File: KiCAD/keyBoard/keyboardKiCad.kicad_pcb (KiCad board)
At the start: 2 copper layers, 356.2 x 133.2 mm, 183 parts, among them SW1 RotaryEncoder_Switch_MP

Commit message: Fixed dimentions of the keyboard PCB, need to update 3D models
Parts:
- moved S83 413.8 mm to (0.00, 0.00)
- moved S80 398.0 mm to (0.00, 0.00)
- moved S82 397.1 mm to (0.00, 0.00)
- moved S81 390.8 mm to (0.00, 0.00)
- moved S79 390.0 mm to (0.00, 0.00)
- moved S76 382.3 mm to (0.00, 0.00)
- moved S78 380.6 mm to (0.00, 0.00)
- moved S77 374.0 mm to (0.00, 0.00)
- moved S75 364.2 mm to (0.00, 0.00)
- moved S74 357.3 mm to (0.00, 0.00)
- moved S69 350.9 mm to (0.00, 0.00)
- moved S63 336.1 mm to (0.00, 0.00)
- moved S68 331.4 mm to (0.00, 0.00)
- moved S72 329.7 mm to (0.00, 0.00)
- moved S64 328.7 mm to (0.00, 0.00)
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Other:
- board size 356.2 x 133.2 mm -> 354 x 132 mm

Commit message: Keyboard routing initially complete
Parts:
- D1, D10, D11, D12, D13, D14, D15, D16, D17, D18, D19, D2, D20, D21, D22, D23, D24, D25, D26, D27, D28, D29, D3, D30, D31, D32, D33, D34, D35, D36, D37, D38, D39, D4, D40, D41, D42, D43, D44, D45, D46, D47, D48, D49, D5, D50, D51, D52, D53, D54, D55, D56, D57, D58, D59, D6, D60, D61, D62, D63, D64, D66, D67, D68, D69, D7, D70, D71, D72, D73, D74, D75, D76, D77, D78, D79, D8, D80, D81, D82, D83, D84, D9: footprint Diode_THT:D_DO-35_SOD27_P10.16mm_Horizontal -> kbProjectLib/lcscImports:DO-35_BD2.0-L4.0-P8.00-D0.5-FD
- S1, S3, S72: footprint PCM_Switch_Keyboard_Kailh:SW_Kailh_Choc_V2_1.50u -> kbProjectLib/keyswitches:SW_Kailh_Choc_V2_1.50u
- S10, S12, S13, S14, S15, S16, S18, S19, S2, S20, S21, S22, S23, S24, S25, S26, S27, S28, S29, S30, S31, S32, S34, S35, S36, S37, S38, S39, S40, S41, S42, S43, S44, S45, S46, S47, S48, S49, S50, S51, S52, S53, S54, S55, S56, S57, S59, S60, S61, S62, S64, S65, S66, S67, S7, S70, S73, S74, S75, S76, S77, S78, S79, S8, S80, S81, S82, S83, S9: footprint PCM_Switch_Keyboard_Kailh:SW_Kailh_Choc_V2_1.00u -> kbProjectLib/keyswitches:SW_Kailh_Choc_V2_1.00u
- S11, S17, S58: footprint PCM_Switch_Keyboard_Kailh:SW_Kailh_Choc_V2_1.25u -> kbProjectLib/keyswitches:SW_Kailh_Choc_V2_1.25u
- S33: footprint PCM_Switch_Keyboard_Kailh:SW_Kailh_Choc_V2_6.25u -> kbProjectLib/keyswitches:SW_Kailh_Choc_V2_6.25u
- S4: footprint PCM_Switch_Keyboard_Kailh:SW_Kailh_Choc_V2_1.75u -> kbProjectLib/keyswitches:SW_Kailh_Choc_V2_1.75u
- S5, S68: footprint PCM_Switch_Keyboard_Kailh:SW_Kailh_Choc_V2_2.25u -> kbProjectLib/keyswitches:SW_Kailh_Choc_V2_2.25u
- S6, S69, S71: footprint PCM_Switch_Keyboard_Kailh:SW_Kailh_Choc_V2_2.00u -> kbProjectLib/keyswitches:SW_Kailh_Choc_V2_2.00u
- S63: footprint PCM_Switch_Keyboard_Kailh:SW_Kailh_Choc_V2_2.75u -> kbProjectLib/keyswitches:SW_Kailh_Choc_V2_2.75u
- SW1: footprint Rotary_Encoder:RotaryEncoder_Alps_EC11E-Switch_Vertical_H20mm -> kbProjectLib/lcscImports:SW-TH_EC11XXXXXXXX
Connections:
- S10 pad 1: ROW4 -> ROW5
- S11 pad 1: ROW5 -> ROW6
- S54 pad 1: ROW1 -> ROW2
- S55 pad 1: ROW2 -> ROW3
- S56 pad 1: ROW3 -> ROW4
- S57 pad 1: ROW4 -> ROW5
- S58 pad 1: ROW5 -> ROW6
- S7 pad 1: ROW1 -> ROW2
- S8 pad 1: ROW2 -> ROW3
- S9 pad 1: ROW3 -> ROW4
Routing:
- net ROW3: track 0.00 -> 335.0 mm
- net ROW1: track 0.00 -> 333.8 mm, vias 0 -> 2
- net ROW2: track 0.00 -> 328.2 mm
- net ROW4: track 0.00 -> 305.4 mm
- net ROW5: track 0.00 -> 244.8 mm
- net ROW6: track 0.00 -> 207.0 mm
- net Net-(D33-A): track 0.00 -> 91.4 mm
- net Net-(D63-A): track 0.00 -> 88.3 mm
- net Net-(D17-A): track 0.00 -> 87.6 mm
- net Net-(D11-A): track 0.00 -> 86.3 mm, vias 0 -> 4
- net Net-(D6-A): track 0.00 -> 85.3 mm
- net Net-(D70-A): track 0.00 -> 84.2 mm
- net Net-(D58-A): track 0.00 -> 80.2 mm
- net Net-(D10-A): track 0.00 -> 78.1 mm
- net Net-(D64-A): track 0.00 -> 76.3 mm, vias 0 -> 2
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
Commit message: saving before running 3d file fixing script
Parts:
- removed H10, H11, H12, H9: ~, ScottoKeebs_Stabilizer:Stabilizer_MX_2.00u
- removed H13, H14: ~, ScottoKeebs_Cutout:Cutout_Stabilizer_3.00u
- removed H15, H16: ~, ScottoKeebs_Stabilizer:Stabilizer_MX_6.25u
- H1, H2, H3, H4, H5, H6: footprint ScottoKeebs_Stabilizer:Stabilizer_MX_2.00u -> kbProjectLib/keyswitches:Stabilizer_Cherry_MX_2.00u
- H7: footprint ScottoKeebs_Stabilizer:Stabilizer_MX_2.00u -> kbProjectLib/keyswitches:Stabilizer_Cherry_MX_3.00u
- H8: footprint ScottoKeebs_Stabilizer:Stabilizer_MX_2.00u -> kbProjectLib/keyswitches:Stabilizer_Cherry_MX_6.25u

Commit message: MCU board has been mounted on to the keyboard PCB. Need to check if spacing is appropriate irl using calipers. Then do mounting holes using star point grounding due to use with metal chassis. ie seperate net found mounting and ground pours, which only connect at the MCU pin.
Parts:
- removed H2, H3, H5, H6: ~, kbProjectLib/keyswitches:Stabilizer_Cherry_MX_2.00u
- added CNN1: ~, kbProjectLib/mcuConnector:keyboardMCU_Connector, F.Cu at (0.00, 0.00)
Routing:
- net rotB: track 0.00 -> 36.0 mm
- net rotC: track 0.00 -> 34.1 mm
- net rotA: track 0.00 -> 32.5 mm
- net Net-(D61-A): track 41.3 -> 39.8 mm

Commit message: Finished routing, including chassis grounding. One thing, I might need SWD for the MCU. QMK should be able to use USB though. Need to check this.
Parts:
- added ? (x17): , , F.Cu at (0.00, 0.00)
- added REF**: MountingHole_3.2mm_M3_Pad, MountingHole:MountingHole_3.2mm_M3_Pad, F.Cu at (0.00, 0.00)
- added REF**: NetTie-2_THT_Pad0.3mm, NetTie:NetTie-2_THT_Pad0.3mm, F.Cu at (0.00, 0.00)
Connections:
- SW1 pad 6: (no net) -> GND
- SW1 pad 7: (no net) -> GND
- SW1 pad D: (no net) -> rotSW
- SW1 pad E: (no net) -> GND
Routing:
- net CHASSIS: track 0.00 -> 977.0 mm
- net COL1: track 20.1 -> 312.2 mm, vias 0 -> 2
- net COL2: track 16.5 -> 266.6 mm
- net COL3: track 20.0 -> 261.0 mm
- net COL4: track 16.5 -> 243.3 mm
- net COL5: track 16.0 -> 228.1 mm, vias 0 -> 3
- net COL6: track 20.0 -> 187.0 mm, vias 0 -> 14
- net COL7: track 16.0 -> 172.1 mm, vias 0 -> 5
- net COL8: track 16.0 -> 167.6 mm, vias 0 -> 11
- net ROW6: track 207.0 -> 334.8 mm, vias 0 -> 10
- net COL9: track 16.1 -> 124.0 mm, vias 0 -> 7
- net ROW5: track 244.8 -> 343.5 mm, vias 0 -> 9
- net COL11: track 16.0 -> 111.9 mm, vias 0 -> 7
- net COL10: track 16.1 -> 111.9 mm, vias 0 -> 5
- net ROW4: track 305.4 -> 387.3 mm, vias 0 -> 7
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- added copper zone on B.Cu, net GND
- added copper zone on F.Cu, net GND

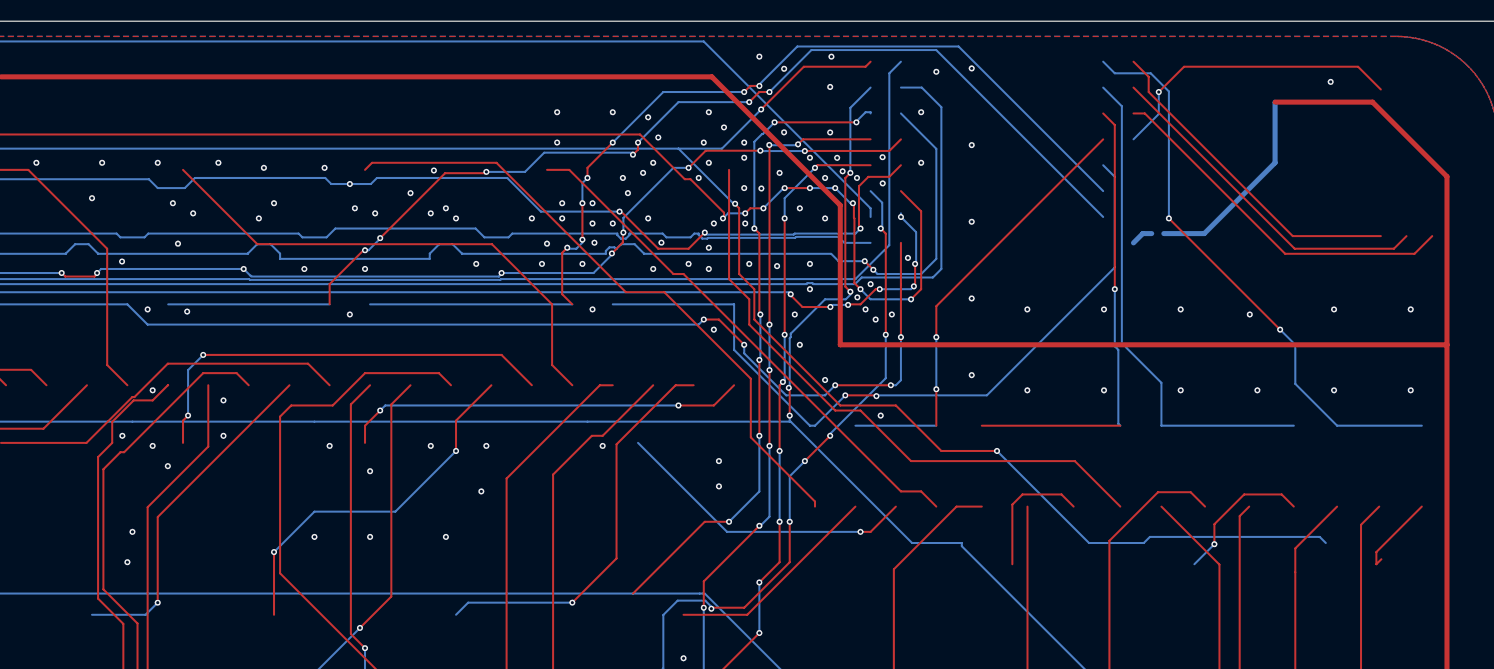
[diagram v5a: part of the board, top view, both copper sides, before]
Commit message: Added SWD connector headers. Touched up routing on both boards.
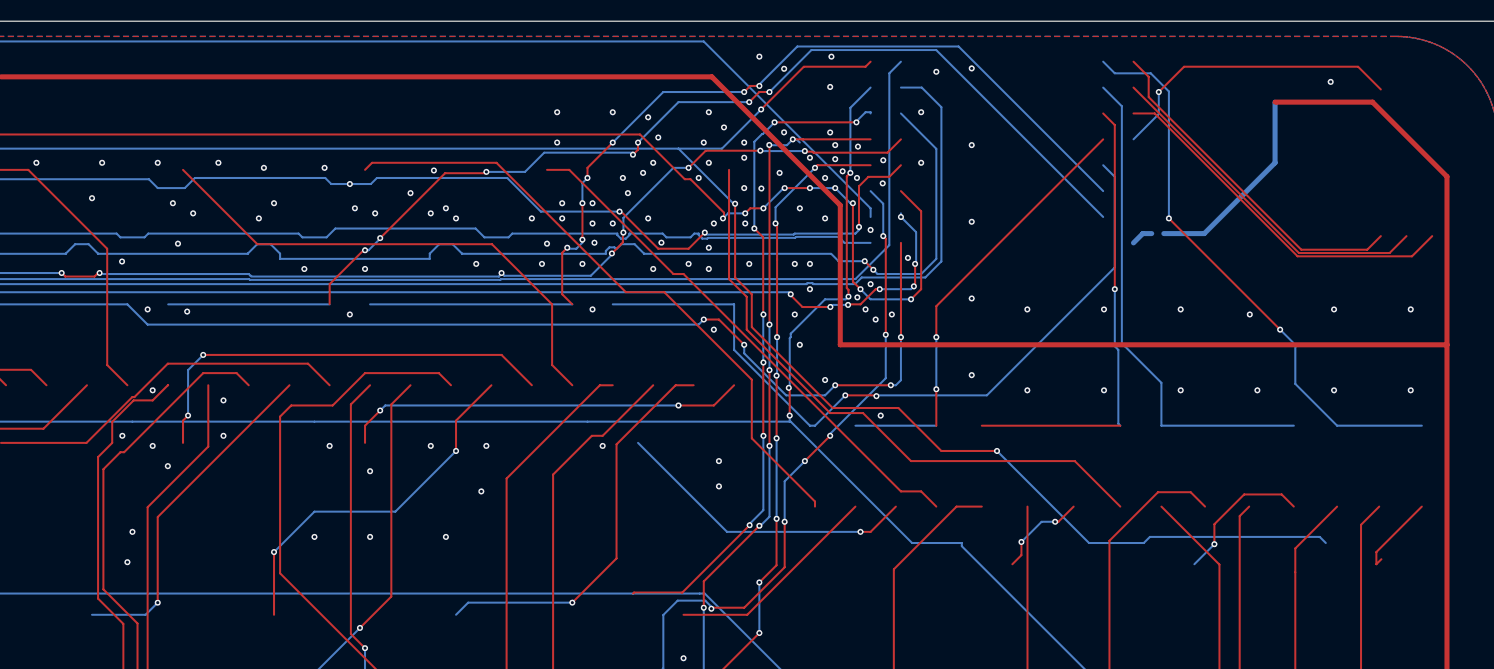
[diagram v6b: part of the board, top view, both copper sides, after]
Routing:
- net Net-(D75-A): track 12.9 -> 9.19 mm, vias 0 -> 2
- net ROW3: track 399.6 -> 401.2 mm
- net rotA: track 32.5 -> 33.9 mm
- net ROW1: track 356.3 -> 356.9 mm
- net ROW4: track 387.3 -> 387.9 mm
- net COL6: track 187.0 -> 187.1 mm, vias 14 -> 13
- net GND: vias 266 -> 269

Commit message: Refining
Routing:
- net GND: vias 269 -> 270
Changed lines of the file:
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@@
 	)
 	(segment
-		(start 343.76 123)
-		(end 343.76 118.76)
+		(start 339.75 91.31)
+		(end 338 89.56)
 		(width 0.2)
 		(layer "B.Cu")
@@
 	)
 	(segment
-		(start 343.76 118.76)
-		(end 339.85 114.85)
+		(start 339.75 114.75)
+		(end 339.75 91.31)
 		(width 0.2)
 		(layer "B.Cu")
@@
 	)
 	(segment
-		(start 339.85 114.85)
-		(end 339.85 91.41)
+		(start 343.76 123)
+		(end 343.76 118.76)
 		(width 0.2)
 		(layer "B.Cu")
@@
 	)
 	(segment
-		(start 339.85 91.41)
-		(end 338 89.56)
+		(start 343.76 118.76)
+		(end 339.75 114.75)
 		(width 0.2)
 		(layer "B.Cu")
@@
 	)
 	(segment
-		(start 339.15 109.5)
-		(end 339.15 115.15)
-		(width 0.2)
-		(layer "B.Cu")
-		(net "COL15")
-	)
-	(segment
-		(start 339.15 115.15)
-		(end 339.5 115.5)
-		(width 0.2)
-		(layer "B.Cu")
-		(net "COL15")
-	)
-	(segment
-		(start 339.5 122.805)
+		(start 339.15 122.455)
 		(end 339.695 123)
 		(width 0.2)
@@
 	)
 	(segment
-		(start 339.5 115.5)
-		(end 339.5 122.805)
+		(start 339.15 109.5)
+		(end 339.15 122.455)
 		(width 0.2)
 		(layer "B.Cu")
@@
 	)
 	(via
+		(at 289.25 107.75)
+		(size 0.6)
+		(drill 0.3)
+		(layers "F.Cu" "B.Cu")
+		(free yes)
+		(net "GND")
+	)
+	(via
 		(at 86.916667 212)
 		(size 0.6)
@@
 	)
 	(segment
-		(start 309.5 130.5)
-		(end 309.5 131)
+		(start 280.875 100.625)
+		(end 285.05 104.8)
 		(width 0.2)
 		(layer "F.Cu")
@@
 	)
 	(segment
-		(start 265 97.7)
-		(end 265.7 97)
+		(start 287.1 106.751471)
+		(end 287.1 106.85)
+		(width 0.2)
+		(layer "F.Cu")
+		(net "Net-(D66-A)")
+	)
+	(segment
+		(start 287.1 106.85)
+		(end 290.05 109.8)
+		(width 0.2)
+		(layer "F.Cu")
+		(net "Net-(D66-A)")
+	)
+	(segment
+		(start 290.05 109.8)
+		(end 294.602943 109.8)
+		(width 0.2)
+		(layer "F.Cu")
+		(net "Net-(D66-A)")
+	)
+	(segment
+		(start 286.65 106.4)
+		(end 286.748529 106.4)
 		(width 0.2)
 		(layer "F.Cu")
@@
 	)
 	(segment
+		(start 303.25 124.25)
+		(end 309.5 130.5)
+		(width 0.2)
+		(layer "F.Cu")
+		(net "Net-(D66-A)")
+	)
+	(segment
+		(start 285.248529 104.8)
+		(end 285.6 105.151471)
+		(width 0.2)
+		(layer "F.Cu")
+		(net "Net-(D66-A)")
+	)
+	(segment
+		(start 279.190864 98.625)
+		(end 280.875 100.309136)
+		(width 0.2)
+		(layer "F.Cu")
+		(net "Net-(D66-A)")
+	)
+	(segment
+		(start 285.05 104.8)
+		(end 285.248529 104.8)
+		(width 0.2)
+		(layer "F.Cu")
+		(net "Net-(D66-A)")
+	)
+	(segment
+		(start 309.5 130.5)
+		(end 309.5 131)
+		(width 0.2)
+		(layer "F.Cu")
+		(net "Net-(D66-A)")
+	)
+	(segment
+		(start 265.7 97)
+		(end 277.25 97)
+		(width 0.2)
+		(layer "F.Cu")
+		(net "Net-(D66-A)")
+	)
+	(segment
+		(start 277.25 97)
+		(end 278.875 98.625)
+		(width 0.2)
+		(layer "F.Cu")
+		(net "Net-(D66-A)")
+	)
+	(segment
+		(start 278.875 98.625)
+		(end 279.190864 98.625)
+		(width 0.2)
+		(layer "F.Cu")
+		(net "Net-(D66-A)")
+	)
+	(segment
 		(start 294.602943 109.8)
 		(end 303.25 118.447057)
@@
 	)
 	(segment
-		(start 278 97)
-		(end 290.8 109.8)
+		(start 280.875 100.309136)
+		(end 280.875 100.625)
 		(width 0.2)
 		(layer "F.Cu")
@@
 	)
 	(segment
-		(start 265.7 97)
-		(end 278 97)
+		(start 285.6 105.151471)
+		(end 285.6 105.35)
 		(width 0.2)
 		(layer "F.Cu")
@@
 	)
 	(segment
-		(start 290.8 109.8)
-		(end 294.602943 109.8)
+		(start 285.6 105.35)
+		(end 286.65 106.4)
 		(width 0.2)
 		(layer "F.Cu")
@@
 	)
 	(segment
-		(start 303.25 124.25)
-		(end 309.5 130.5)
+		(start 286.748529 106.4)
+		(end 287.1 106.751471)
+		(width 0.2)
+		(layer "F.Cu")
+		(net "Net-(D66-A)")
+	)
+	(segment
+		(start 265 97.7)
+		(end 265.7 97)
 		(width 0.2)
 		(layer "F.Cu")
